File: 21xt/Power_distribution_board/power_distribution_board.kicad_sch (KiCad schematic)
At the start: 25 parts, among them IC1 LM74700QDBVRQ1, IC2 LM74700QDBVRQ1, IC3 LTC2959IDDB#TRMPBF, IC4 INA180A1IDBVR, IC5 TLV76150DCYR, J1 Conn_01x04, J2 Conn_01x02, Q1 NVMFWS2D1N08XT1G, Q2 NVMFWS2D1N08XT1G, U1 esp32 c6 xiao

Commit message: redone schematic
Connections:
- no-connect marks 10 -> 9
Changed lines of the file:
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@@
-	)
-	(no_connect
-		(at 53.34 172.72)
 	)
 	(no_connect

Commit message: aaa
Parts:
- removed J1: Conn_01x04, Connector:FanPinHeader_1x04_P2.54mm_Vertical, symbol Connector_Generic:Conn_01x04
- added J3, J4: Conn_01x02, 21xt_footprints:Deans Connector Male, symbol Connector_Generic:Conn_01x02
- J2: footprint 21xt_footprints:PinHeader_1x02_P2.54mm_Vertical -> 21xt_footprints:Deans Connector Male
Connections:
- net B1+: now also J4.1 (Pin_1)
- net B2+: now also J3.1 (Pin_1)
- net GND: now also J3.2 (Pin_2), J4.2 (Pin_2)
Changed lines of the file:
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@@
+	(wire
+		(pts
+			(xy 52.07 120.65) (xy 52.07 128.27)
+		)
+		(stroke
+			(width 0)
+			(type default)
+		)
+	)
 	(wire
 		(pts
@@
 		)
 	)
+	(global_label "B2-"
+		(shape input)
+		(at 25.4 88.9 0)
+		(fields_autoplaced yes)
+		(effects
+			(font
+				(size 1.27 1.27)
+			)
+			(justify left)
+		)
+		(property "Intersheetrefs" "${INTERSHEET_REFS}"
+			(at 31.7829 88.9 0)
+			(effects
+				(font
+					(size 1.27 1.27)
+				)
+				(justify left)
+				(hide yes)
+			)
+		)
+	)
 	(global_label "V_OR_Supply"
 		(shape input)
@@
 		)
 	)
-	(global_label "B2-"
+	(global_label "B1+"
 		(shape input)
-		(at 25.4 110.49 0)
+		(at 25.4 82.55 0)
 		(fields_autoplaced yes)
 		(effects
@@
 		)
 		(property "Intersheetrefs" "${INTERSHEET_REFS}"
-			(at 31.7829 110.49 0)
+			(at 31.7829 82.55 0)
 			(effects
 				(font
@@
 		)
 	)
-	(global_label "B2+"
+	(global_label "B1-"
 		(shape input)
-		(at 25.4 107.95 0)
+		(at 25.4 80.01 0)
 		(fields_autoplaced yes)
 		(effects
@@
 		)
 		(property "Intersheetrefs" "${INTERSHEET_REFS}"
-			(at 31.7829 107.95 0)
+			(at 31.7829 80.01 0)
 			(effects
 				(font
@@
 		)
 	)
-	(global_label "B1+"
-		(shape input)
-		(at 25.4 105.41 0)
-		(fields_autoplaced yes)
-		(effects
-			(font
-				(size 1.27 1.27)
-			)
-			(justify left)
-		)
-		(property "Intersheetrefs" "${INTERSHEET_REFS}"
-			(at 31.7829 105.41 0)
-			(effects
-				(font
-					(size 1.27 1.27)
-				)
-				(justify left)
-				(hide yes)
-			)
-		)
-	)
 	(global_label "B2-"
 		(shape input)
@@
 	(global_label "B2+"
 		(shape input)
+		(at 25.4 91.44 0)
+		(fields_autoplaced yes)
+		(effects
+			(font
+				(size 1.27 1.27)
+			)
+			(justify left)
+		)
+		(property "Intersheetrefs" "${INTERSHEET_REFS}"
+			(at 31.7829 91.44 0)
+			(effects
+				(font
+					(size 1.27 1.27)
+				)
+				(justify left)
+				(hide yes)
+			)
+		)
+	)
+	(global_label "B2+"
+		(shape input)
 		(at 125.73 93.98 0)
 		(fields_autoplaced yes)
@@
 		)
 	)
-	(global_label "B1-"
-		(shape input)
-		(at 25.4 102.87 0)
-		(fields_autoplaced yes)
-		(effects
-			(font
-				(size 1.27 1.27)
-			)
-			(justify left)
-		)
-		(property "Intersheetrefs" "${INTERSHEET_REFS}"
-			(at 31.7829 102.87 0)
-			(effects
-				(font
-					(size 1.27 1.27)
-				)
-				(justify left)
-				(hide yes)
-			)
-		)
-	)
 	(global_label "SCL"
 		(shape bidirectional)
@@
 				(justify right)
 				(hide yes)
+			)
+		)
+	)
+	(symbol
+		(lib_id "Connector_Generic:Conn_01x02")
+		(at 20.32 82.55 180)
+		(unit 1)
+		(exclude_from_sim no)
+		(in_bom yes)
+		(on_board yes)
+		(dnp no)
+		(fields_autoplaced yes)
+		(property "Reference" "J4"
+			(at 20.32 73.66 0)
+			(effects
+				(font
+					(size 1.27 1.27)
+				)
+			)
+		)
+		(property "Value" "Conn_01x02"
+			(at 20.32 76.2 0)
+			(effects
+				(font
+					(size 1.27 1.27)
+				)
+			)
+		)
+		(property "Footprint" "21xt_footprints:Deans Connector Male"
+			(at 20.32 82.55 0)
+			(effects
+				(font
+					(size 1.27 1.27)
+				)
+				(hide yes)
+			)
+		)
+		(property "Datasheet" "~"
+			(at 20.32 82.55 0)
+			(effects
+				(font
+					(size 1.27 1.27)
+				)
+				(hide yes)
+			)
+		)
+		(property "Description" "Generic connector, single row, 01x02, script generated (kicad-library-utils/schlib/autogen/connector/)"
+			(at 20.32 82.55 0)
+			(effects
+				(font
+					(size 1.27 1.27)
+				)
+				(hide yes)
+			)
+		)
+		(pin "1"
+		)
+		(pin "2"
+		)
+		(instances
+			(project "power_distribution_board"
+				(path "/d98247d4-72eb-44af-93af-b1e95cbdd104"
+					(reference "J4")
+					(unit 1)
+				)
 			)
 		)
@@
 	)
 	(symbol
-		(lib_id "power:PWR_FLAG")
-		(at 25.4 107.95 0)
-		(unit 1)
-		(exclude_from_sim no)
-		(in_bom yes)
-		(on_board yes)
-		(dnp no)
-		(fields_autoplaced yes)
-		(property "Reference" "#FLG03"
-			(at 25.4 106.045 0)
-			(effects
-				(font
-					(size 1.27 1.27)
-				)
-				(hide yes)
-			)
-		)
-		(property "Value" "PWR_FLAG"
-			(at 25.4 102.87 0)
-			(effects
-				(font
-					(size 1.27 1.27)
-				)
-			)
-		)
-		(property "Footprint" ""
-			(at 25.4 107.95 0)
-			(effects
-				(font
-					(size 1.27 1.27)
-				)
-				(hide yes)
-			)
-		)
-		(property "Datasheet" "~"
-			(at 25.4 107.95 0)
-			(effects
-				(font
-					(size 1.27 1.27)
-				)
-				(hide yes)
-			)
-		)
-		(property "Description" "Special symbol for telling ERC where power comes from"
-			(at 25.4 107.95 0)
-			(effects
-				(font
-					(size 1.27 1.27)
-				)
-				(hide yes)
-			)
-		)
-		(pin "1"
-		)
-		(instances
-			(project "power_distribution_board"
-				(path "/d98247d4-72eb-44af-93af-b1e95cbdd104"
-					(reference "#FLG03")
-					(unit 1)
-				)
-			)
-		)
-	)
-	(symbol
 		(lib_id "Device:C")
 		(at 109.22 45.72 0)
@@
 	)
 	(symbol
-		(lib_id "Connector_Generic:Conn_01x04")
-		(at 20.32 107.95 180)
+		(lib_id "Connector_Generic:Conn_01x02")
+		(at 20.32 91.44 180)
 		(unit 1)
 		(exclude_from_sim no)
@@
 		(dnp no)
 		(fields_autoplaced yes)
-		(property "Reference" "J1"
-			(at 20.32 96.52 0)
-			(effects
-				(font
-					(size 1.27 1.27)
-				)
-			)
-		)
-		(property "Value" "Conn_01x04"
-			(at 20.32 99.06 0)
-			(effects
-				(font
-					(size 1.27 1.27)
-				)
-			)
-		)
-		(property "Footprint" "Connector:FanPinHeader_1x04_P2.54mm_Vertical"
-			(at 20.32 107.95 0)
+		(property "Reference" "J3"
+			(at 20.32 82.55 0)
+			(effects
+				(font
+					(size 1.27 1.27)
+				)
+			)
+		)
+		(property "Value" "Conn_01x02"
+			(at 20.32 85.09 0)
+			(effects
+				(font
+					(size 1.27 1.27)
+				)
+			)
+		)
+		(property "Footprint" "21xt_footprints:Deans Connector Male"
+			(at 20.32 91.44 0)
 			(effects
 				(font
@@
 		)
 		(property "Datasheet" "~"
-			(at 20.32 107.95 0)
-			(effects
-				(font
-					(size 1.27 1.27)
-				)
-				(hide yes)
-			)
-		)
-		(property "Description" "Generic connector, single row, 01x04, script generated (kicad-library-utils/schlib/autogen/connector/)"
-			(at 20.32 107.95 0)
-			(effects
-				(font
-					(size 1.27 1.27)
-				)
-				(hide yes)
-			)
+			(at 20.32 91.44 0)
+			(effects
+				(font
+					(size 1.27 1.27)
+				)
+				(hide yes)
+			)
+		)
+		(property "Description" "Generic connector, single row, 01x02, script generated (kicad-library-utils/schlib/autogen/connector/)"
+			(at 20.32 91.44 0)
+			(effects
+				(font
+					(size 1.27 1.27)
+				)
+				(hide yes)
+			)
+		)
+		(pin "1"
 		)
 		(pin "2"
 		)
-		(pin "3"
-		)
-		(pin "4"
-		)
-		(pin "1"
-		)
 		(instances
-			(project ""
+			(project "power_distribution_board"
 				(path "/d98247d4-72eb-44af-93af-b1e95cbdd104"
-					(reference "J1")
+					(reference "J3")
 					(unit 1)
 				)
@@
 	)
 	(symbol
-		(lib_id "power:PWR_FLAG")
-		(at 25.4 105.41 0)
-		(unit 1)
-		(exclude_from_sim no)
-		(in_bom yes)
-		(on_board yes)
-		(dnp no)
-		(fields_autoplaced yes)
-		(property "Reference" "#FLG02"
-			(at 25.4 103.505 0)
-			(effects
-				(font
-					(size 1.27 1.27)
-				)
-				(hide yes)
-			)
-		)
-		(property "Value" "PWR_FLAG"
-			(at 25.4 100.33 0)
-			(effects
-				(font
-					(size 1.27 1.27)
-				)
-			)
-		)
-		(property "Footprint" ""
-			(at 25.4 105.41 0)
-			(effects
-				(font
-					(size 1.27 1.27)
-				)
-				(hide yes)
-			)
-		)
-		(property "Datasheet" "~"
-			(at 25.4 105.41 0)
-			(effects
-				(font
-					(size 1.27 1.27)
-				)
-				(hide yes)
-			)
-		)
-		(property "Description" "Special symbol for telling ERC where power comes from"
-			(at 25.4 105.41 0)
-			(effects
-				(font
-					(size 1.27 1.27)
-				)
-				(hide yes)
-			)
-		)
-		(pin "1"
-		)
-		(instances
-			(project "power_distribution_board"
-				(path "/d98247d4-72eb-44af-93af-b1e95cbdd104"
-					(reference "#FLG02")
-					(unit 1)
-				)
-			)
-		)
-	)
-	(symbol
 		(lib_id "21xt_symbols:LTC2959IDDB#TRMPBF")
 		(at 213.36 55.88 0)
@@
 			)
 		)
-		(property "Footprint" "21xt_footprints:PinHeader_1x02_P2.54mm_Vertical"
+		(property "Footprint" "21xt_footprints:Deans Connector Male"
 			(at 20.32 125.73 0)
 			(effects

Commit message: asdf
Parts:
- added H1, H2: MountingHole, MountingHole:MountingHole_3.2mm_M3, symbol Mechanical:MountingHole
- R1: footprint Resistor_SMD:R_0805_2012Metric -> 21xt_footprints:R_0603_1608Metric_Pad0.98x0.95mm_HandSolder
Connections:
- net GND: now also J2.2 (Pin_2); no longer J2.1 (Pin_1)
- net V_OUT_Supply: now also J2.1 (Pin_1); no longer J2.2 (Pin_2)
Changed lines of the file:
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@@
 		)
 	)
+	(global_label "V_OUT_Supply"
+		(shape input)
+		(at 25.4 125.73 0)
+		(fields_autoplaced yes)
+		(effects
+			(font
+				(size 1.27 1.27)
+			)
+			(justify left)
+		)
+		(property "Intersheetrefs" "${INTERSHEET_REFS}"
+			(at 40.6727 125.73 0)
+			(effects
+				(font
+					(size 1.27 1.27)
+				)
+				(justify left)
+				(hide yes)
+			)
+		)
+	)
 	(global_label "V_OR_Supply"
 		(shape output)
@@
 		)
 	)
-	(global_label "V_OUT_Supply"
-		(shape input)
-		(at 25.4 123.19 0)
-		(fields_autoplaced yes)
-		(effects
-			(font
-				(size 1.27 1.27)
-			)
-			(justify left)
-		)
-		(property "Intersheetrefs" "${INTERSHEET_REFS}"
-			(at 40.6727 123.19 0)
-			(effects
-				(font
-					(size 1.27 1.27)
-				)
-				(justify left)
-				(hide yes)
-			)
-		)
-	)
 	(global_label "5V_Regulator"
 		(shape input)
@@
 	)
 	(symbol
-		(lib_id "power:GND")
-		(at 25.4 125.73 90)
-		(unit 1)
-		(exclude_from_sim no)
-		(in_bom yes)
-		(on_board yes)
-		(dnp no)
-		(property "Reference" "#PWR015"
-			(at 31.75 125.73 0)
-			(effects
-				(font
-					(size 1.27 1.27)
-				)
-				(hide yes)
-			)
-		)
-		(property "Value" "GND"
-			(at 28.448 124.714 90)
-			(effects
-				(font
-					(size 1.27 1.27)
-				)
-				(justify right)
-			)
-		)
-		(property "Footprint" ""
-			(at 25.4 125.73 0)
-			(effects
-				(font
-					(size 1.27 1.27)
-				)
-				(hide yes)
-			)
-		)
-		(property "Datasheet" ""
-			(at 25.4 125.73 0)
-			(effects
-				(font
-					(size 1.27 1.27)
-				)
-				(hide yes)
-			)
-		)
-		(property "Description" "Power symbol creates a global label with name \"GND\" , ground"
-			(at 25.4 125.73 0)
-			(effects
-				(font
-					(size 1.27 1.27)
-				)
-				(hide yes)
-			)
-		)
-		(pin "1"
-		)
-		(instances
-			(project "power_distribution_board"
-				(path "/d98247d4-72eb-44af-93af-b1e95cbdd104"
-					(reference "#PWR015")
-					(unit 1)
-				)
-			)
-		)
-	)
-	(symbol
 		(lib_id "Device:R")
 		(at 220.98 135.89 90)
@@
 			)
 		)
-		(property "Footprint" "Resistor_SMD:R_0805_2012Metric"
+		(property "Footprint" "21xt_footprints:R_0603_1608Metric_Pad0.98x0.95mm_HandSolder"
 			(at 220.98 137.668 90)
 			(effects
@@
 	)
 	(symbol
+		(lib_id "power:GND")
+		(at 25.4 123.19 90)
+		(unit 1)
+		(exclude_from_sim no)
+		(in_bom yes)
+		(on_board yes)
+		(dnp no)
+		(property "Reference" "#PWR015"
+			(at 31.75 123.19 0)
+			(effects
+				(font
+					(size 1.27 1.27)
+				)
+				(hide yes)
+			)
+		)
+		(property "Value" "GND"
+			(at 28.448 122.174 90)
+			(effects
+				(font
+					(size 1.27 1.27)
+				)
+				(justify right)
+			)
+		)
+		(property "Footprint" ""
+			(at 25.4 123.19 0)
+			(effects
+				(font
+					(size 1.27 1.27)
+				)
+				(hide yes)
+			)
+		)
+		(property "Datasheet" ""
+			(at 25.4 123.19 0)
+			(effects
+				(font
+					(size 1.27 1.27)
+				)
+				(hide yes)
+			)
+		)
+		(property "Description" "Power symbol creates a global label with name \"GND\" , ground"
+			(at 25.4 123.19 0)
+			(effects
+				(font
+					(size 1.27 1.27)
+				)
+				(hide yes)
+			)
+		)
+		(pin "1"
+		)
+		(instances
+			(project "power_distribution_board"
+				(path "/d98247d4-72eb-44af-93af-b1e95cbdd104"
+					(reference "#PWR015")
+					(unit 1)
+				)
+			)
+		)
+	)
+	(symbol
 		(lib_id "21xt_symbols:LTC2959IDDB#TRMPBF")
 		(at 213.36 55.88 0)
@@
 	)
 	(symbol
+		(lib_id "Mechanical:MountingHole")
+		(at 25.4 30.48 0)
+		(unit 1)
+		(exclude_from_sim yes)
+		(in_bom no)
+		(on_board yes)
+		(dnp no)
+		(fields_autoplaced yes)
+		(property "Reference" "H1"
+			(at 27.94 29.2099 0)
+			(effects
+				(font
+					(size 1.27 1.27)
+				)
+				(justify left)
+			)
+		)
+		(property "Value" "MountingHole"
+			(at 27.94 31.7499 0)
+			(effects
+				(font
+					(size 1.27 1.27)
+				)
+				(justify left)
+			)
+		)
+		(property "Footprint" "MountingHole:MountingHole_3.2mm_M3"
+			(at 25.4 30.48 0)
+			(effects
+				(font
+					(size 1.27 1.27)
+				)
+				(hide yes)
+			)
+		)
+		(property "Datasheet" "~"
+			(at 25.4 30.48 0)
+			(effects
+				(font
+					(size 1.27 1.27)
+				)
+				(hide yes)
+			)
+		)
+		(property "Description" "Mounting Hole without connection"
+			(at 25.4 30.48 0)
+			(effects
+				(font
+					(size 1.27 1.27)
+				)
+				(hide yes)
+			)
+		)
+		(instances
+			(project ""
+				(path "/d98247d4-72eb-44af-93af-b1e95cbdd104"
+					(reference "H1")
+					(unit 1)
+				)
+			)
+		)
+	)
+	(symbol
 		(lib_id "Device:C")
 		(at 60.96 50.8 0)
@@
 					(unit 1)
 				)
+			)
+		)
+	)
+	(symbol
+		(lib_id "Mechanical:MountingHole")
+		(at 43.18 30.48 0)
+		(unit 1)
+		(exclude_from_sim yes)
+		(in_bom no)
+		(on_board yes)
+		(dnp no)
+		(fields_autoplaced yes)
+		(property "Reference" "H2"
+			(at 45.72 29.2099 0)
+			(effects
+				(font
+					(size 1.27 1.27)
+				)
+				(justify left)
+			)
+		)
+		(property "Value" "MountingHole"
+			(at 45.72 31.7499 0)
+			(effects
+				(font
+					(size 1.27 1.27)
+				)
+				(justify left)
+			)
+		)
+		(property "Footprint" "MountingHole:MountingHole_3.2mm_M3"
+			(at 43.18 30.48 0)
+			(effects
+				(font
+					(size 1.27 1.27)
+				)
+				(hide yes)
+			)
+		)
+		(property "Datasheet" "~"
+			(at 43.18 30.48 0)
+			(effects
+				(font
+					(size 1.27 1.27)
+				)
+				(hide yes)
+			)
+		)
+		(property "Description" "Mounting Hole without connection"
+			(at 43.18 30.48 0)
+			(effects
+				(font
+					(size 1.27 1.27)
+				)
+				(hide yes)
+			)
+		)
+		(instances
+			(project "power_distribution_board"
+				(path "/d98247d4-72eb-44af-93af-b1e95cbdd104"
+					(reference "H2")
+					(unit 1)
+				)

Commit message: aaaa
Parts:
- R1: footprint 21xt_footprints:R_0603_1608Metric_Pad0.98x0.95mm_HandSolder -> hi:RESC_WSHM2818R0150FEA
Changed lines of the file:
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@@
 			)
 		)
-		(property "Footprint" "21xt_footprints:R_0603_1608Metric_Pad0.98x0.95mm_HandSolder"
+		(property "Footprint" "hi:RESC_WSHM2818R0150FEA"
 			(at 220.98 137.668 90)
 			(effects

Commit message: aaa
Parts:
- added J1, J5: Conn_01x02, 21xt_footprints:Deans Connector Female, symbol Connector_Generic:Conn_01x02
- J2: footprint 21xt_footprints:Deans Connector Male -> 21xt_footprints:Deans Connector Female
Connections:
- net GND: now also J1.2 (Pin_2), J5.2 (Pin_2)
- net V_OUT_Supply: now also J1.1 (Pin_1), J5.1 (Pin_1)

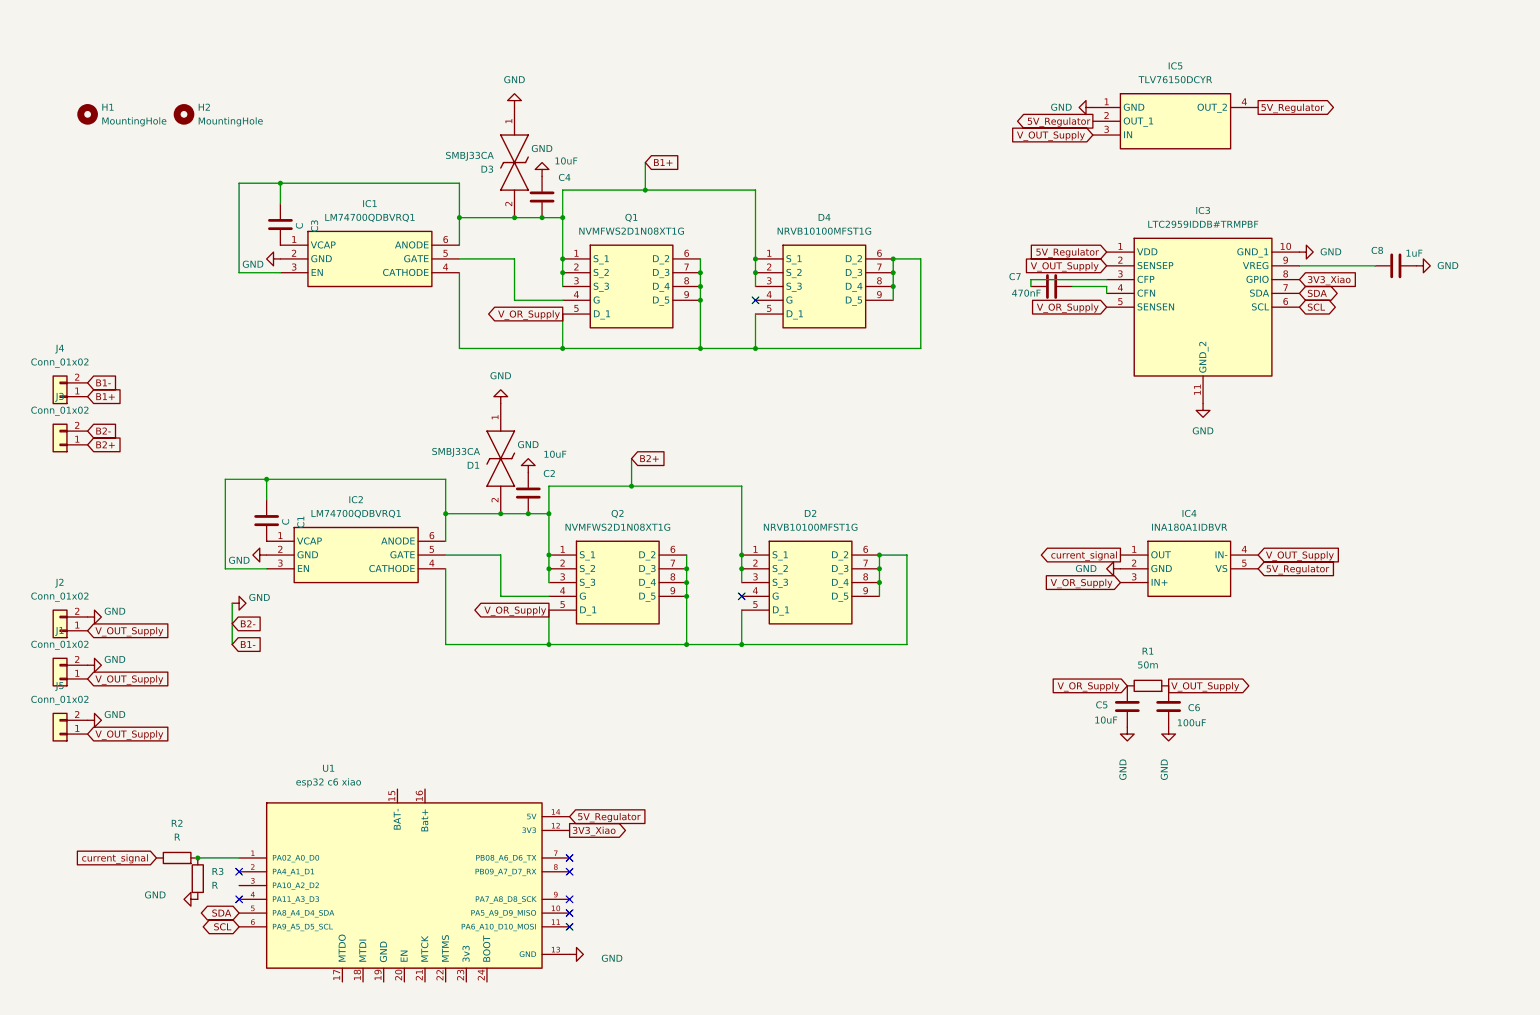
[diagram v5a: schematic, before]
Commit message: add uvlo
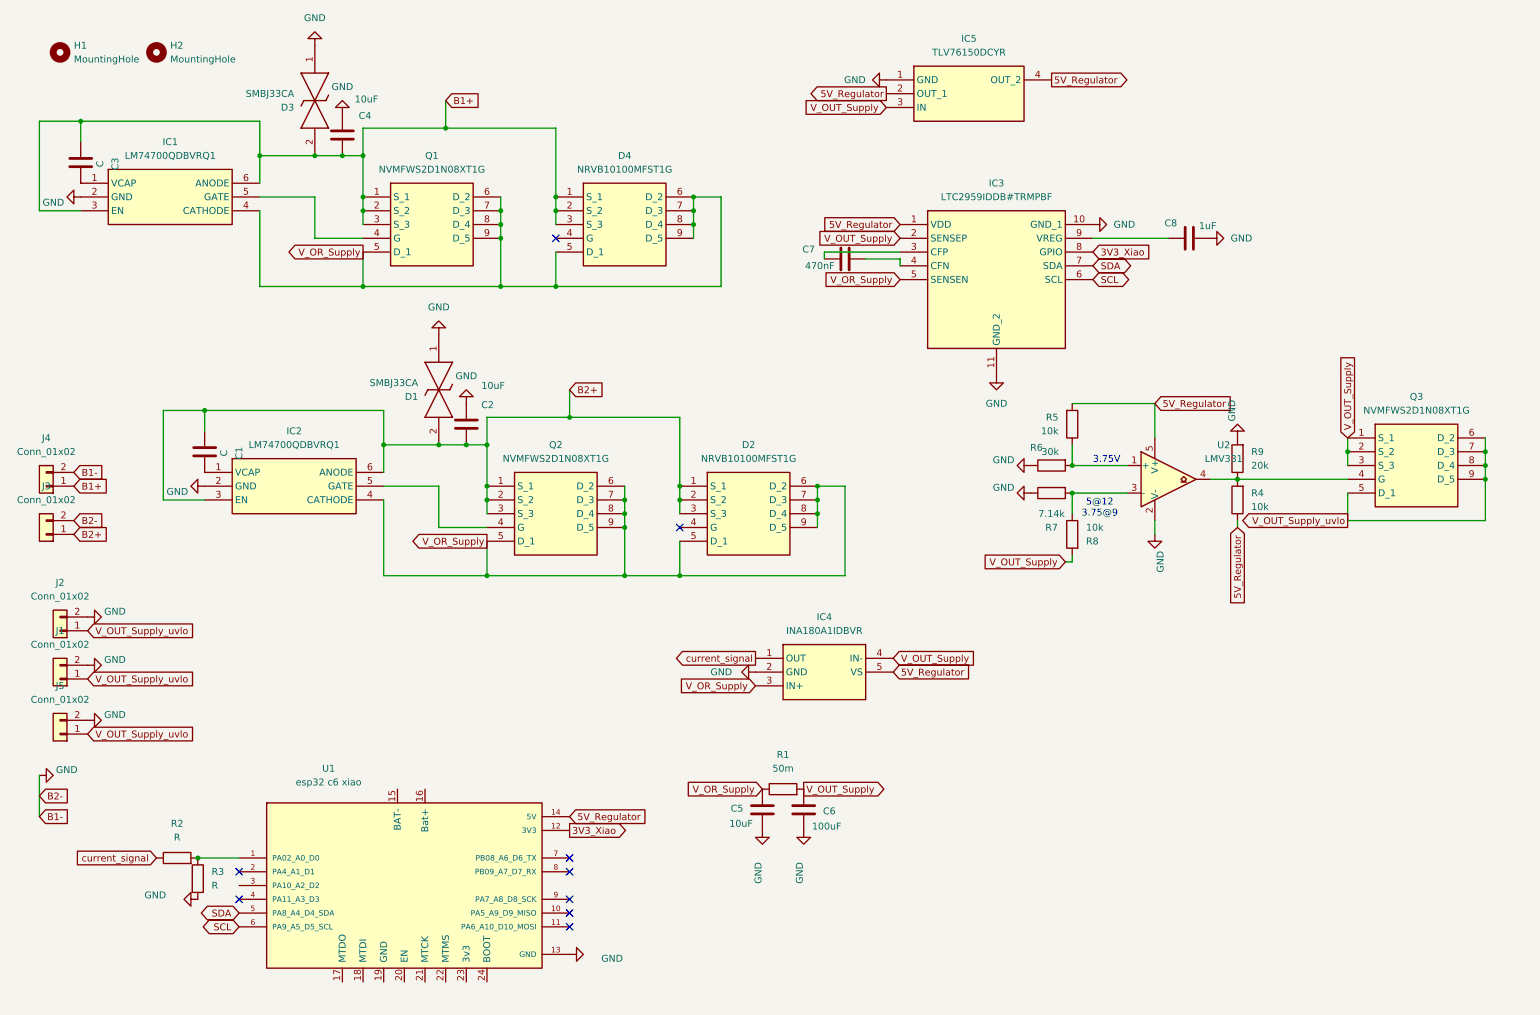
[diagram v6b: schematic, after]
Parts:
- added Q3: NVMFWS2D1N08XT1G, 21xt_footprints:NTMFWS1D5N08XT1G, symbol 21xt_symbols:NVMFWS2D1N08XT1G
- added R4, R5, R8: 10k, Resistor_SMD:R_0402_1005Metric, symbol Device:R
- added R6: 30k, Resistor_SMD:R_0402_1005Metric, symbol Device:R
- added R7: 7.14k, Resistor_SMD:R_0402_1005Metric, symbol Device:R
- added R9: 20k, Resistor_SMD:R_0402_1005Metric, symbol Device:R
- added U2: LMV331, Package_TO_SOT_SMD:SOT-23-5, symbol Comparator:LMV331
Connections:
- net 5V_Regulator: now also R4.1, R5.2, U2.5 (V+)
- net GND: now also R6.1, R7.1, R9.2, U2.2 (V-)
- net V_OUT_Supply: now also Q3.1 (S_1), Q3.2 (S_2), Q3.3 (S_3), R8.2; no longer J1.1 (Pin_1), J2.1 (Pin_1), J5.1 (Pin_1)
- new net: R5.1, R6.2, U2.1 (+)
- new net: Q3.4 (G), R4.2, R9.1, U2.4
- new net: R7.2, R8.1, U2.3 (-)
- new net V_OUT_Supply_uvlo: J1.1 (Pin_1), J2.1 (Pin_1), J5.1 (Pin_1), Q3.5 (D_1), Q3.6 (D_2), Q3.7 (D_3), Q3.8 (D_4), Q3.9 (D_5)
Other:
- note added: "3.75V"
- note added: "5@12 3.75@9"
- moved on the sheet: C1, C2, C3, C4, C5, C6, C7, C8, D1, D2, D3, D4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
